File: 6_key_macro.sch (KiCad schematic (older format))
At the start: 39 parts, among them J1 SWD, P1 USB_C_Plug_USB2.0, Q1 DMG1012T, SW1 CherryMX_LED, SW2 CherryMX_LED, SW3 CherryMX_LED, SW4 CherryMX_LED, SW5 CherryMX_LED, SW6 CherryMX_LED, SW7 Boot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

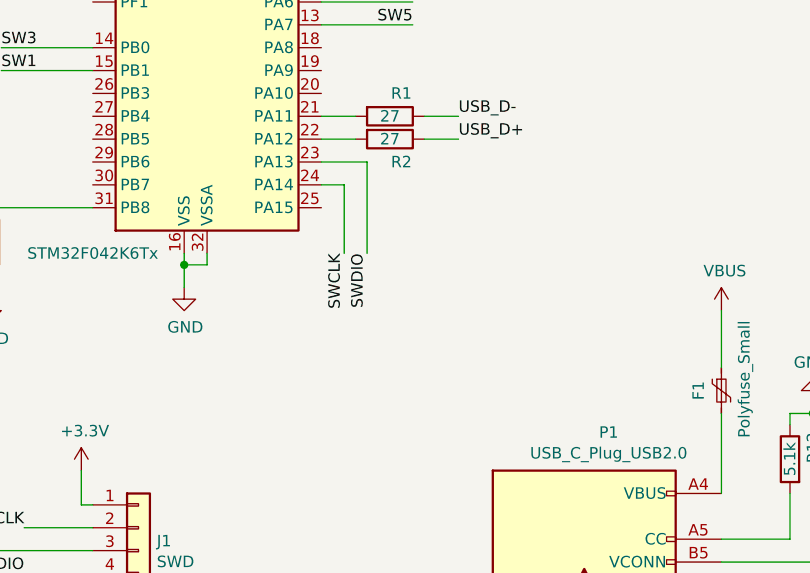
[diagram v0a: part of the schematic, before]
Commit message: moved files to top level. Decided to move firmware to separate repo
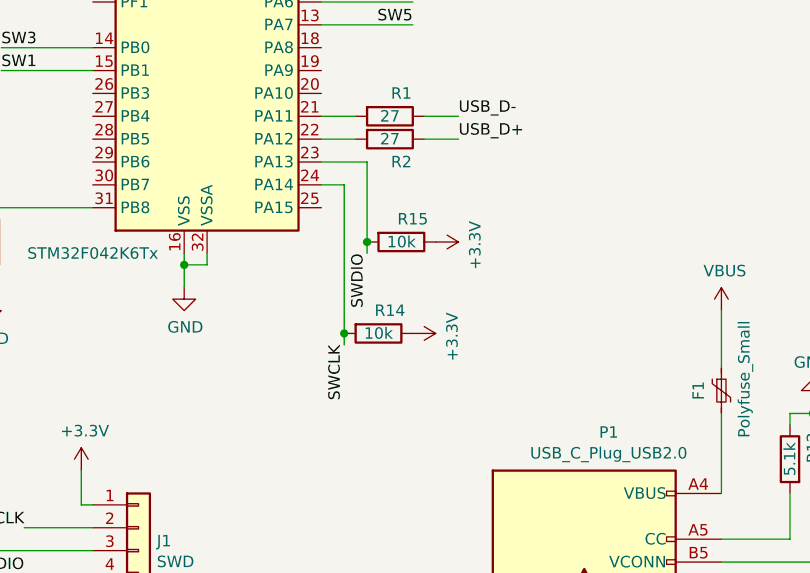
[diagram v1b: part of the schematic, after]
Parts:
- added R14, R15: 10k, Resistor_SMD:R_0805_2012Metric_Pad1.20x1.40mm_HandSolder, symbol Device:R
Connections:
- net +3V3: now also R14.1, R15.1
- net SWCLK: now also R14.2
- net SWDIO: now also R15.2
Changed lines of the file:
@@
 Text Label 2850 4650 3    50   ~ 0
 SWDIO
-Text Label 2750 4650 3    50   ~ 0
+Text Label 2750 5050 3    50   ~ 0
 SWCLK
 Wire Wire Line
-	2750 4650 2750 4350
-Wire Wire Line
 	2650 4350 2750 4350
 Wire Wire Line
 	2850 4250 2650 4250
 Wire Wire Line
-	2850 4250 2850 4650
+	2850 4250 2850 4600
 $Comp
 L Device:R R10
@@
 	0    1    1    0
 $EndComp
+Wire Wire Line
+	2750 4350 2750 5000
+$Comp
+L power:+3.3V #PWR0132
+U 1 1 61852197
+P 3150 4600
+F 0 "#PWR0132" H 3150 4450 50  0001 C CNN
+F 1 "+3.3V" H 3165 4773 50  0000 C CNN
+F 2 "" H 3150 4600 50  0001 C CNN
+F 3 "" H 3150 4600 50  0001 C CNN
+	1    3150 4600
+	0    1    1    0
+$EndComp
+$Comp
+L Device:R R14
+U 1 1 61852CCA
+P 2900 5000
+F 0 "R14" V 2800 5050 50  0000 C CNN
+F 1 "10k" V 2900 5000 50  0000 C CNN
+F 2 "Resistor_SMD:R_0805_2012Metric_Pad1.20x1.40mm_HandSolder" V 2830 5000 50  0001 C CNN
+F 3 "~" H 2900 5000 50  0001 C CNN
+	1    2900 5000
+	0    1    1    0
+$EndComp
+Connection ~ 2750 5000
+Wire Wire Line
+	2750 5000 2750 5050
+$Comp
+L Device:R R15
+U 1 1 61853C73
+P 3000 4600
+F 0 "R15" V 2900 4650 50  0000 C CNN
+F 1 "10k" V 3000 4600 50  0000 C CNN
+F 2 "Resistor_SMD:R_0805_2012Metric_Pad1.20x1.40mm_HandSolder" V 2930 4600 50  0001 C CNN
+F 3 "~" H 3000 4600 50  0001 C CNN
+	1    3000 4600
+	0    1    1    0
+$EndComp
+Connection ~ 2850 4600
+Wire Wire Line
+	2850 4600 2850 4650
+$Comp
+L power:+3.3V #PWR0133
+U 1 1 61854335
+P 3050 5000
+F 0 "#PWR0133" H 3050 4850 50  0001 C CNN
+F 1 "+3.3V" H 3065 5173 50  0000 C CNN
+F 2 "" H 3050 5000 50  0001 C CNN
+F 3 "" H 3050 5000 50  0001 C CNN
+	1    3050 5000
+	0    1    1    0
+$EndComp
